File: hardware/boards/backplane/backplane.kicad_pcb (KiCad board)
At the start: 2 copper layers, 47 parts, among them J1 SPARE_I2C, J10 I2C_IN, J11 I2C_OUT, J12 LED_EXT_OUT, J14 DC_IN, J2 SLOT_4, J3 SLOT_1, J4 SLOT_2, J5 SLOT_5, J6 SLOT_6, J7 SLOT_3, J8 LED_EXT_IN, U1 TCA9548APWR, U2 USBLC6-2SC6, U3 USBLC6-2SC6, U4 USBLC6-2SC6, U5 USBLC6-2SC6, U6 USBLC6-2SC6, U7 USBLC6-2SC6

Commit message: Save current PCB layout edits
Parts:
- moved J12 214.8 mm to (196.5, 70.1)
- moved J11 213.7 mm to (196.6, 51.5)
- moved J1 86.8 mm to (54.2, 13.3)
- moved JP3 69.4 mm to (60.3, 32.1), turned to 180 degrees
- moved JP2 67.3 mm to (60.4, 36.2), turned to 180 degrees
- moved JP1 66.9 mm to (60.6, 40.2), turned to 180 degrees
- moved C1 65.8 mm to (57.3, 27.9)
- moved U1 54.3 mm to (52.5, 34.9)
- moved J10 46.0 mm to (19.1, 42.5), turned to 90 degrees
- moved J8 44.3 mm to (20.2, 49.5), turned to 90 degrees
- moved R1 43.2 mm to (45.8, 31.1), turned to -90 degrees

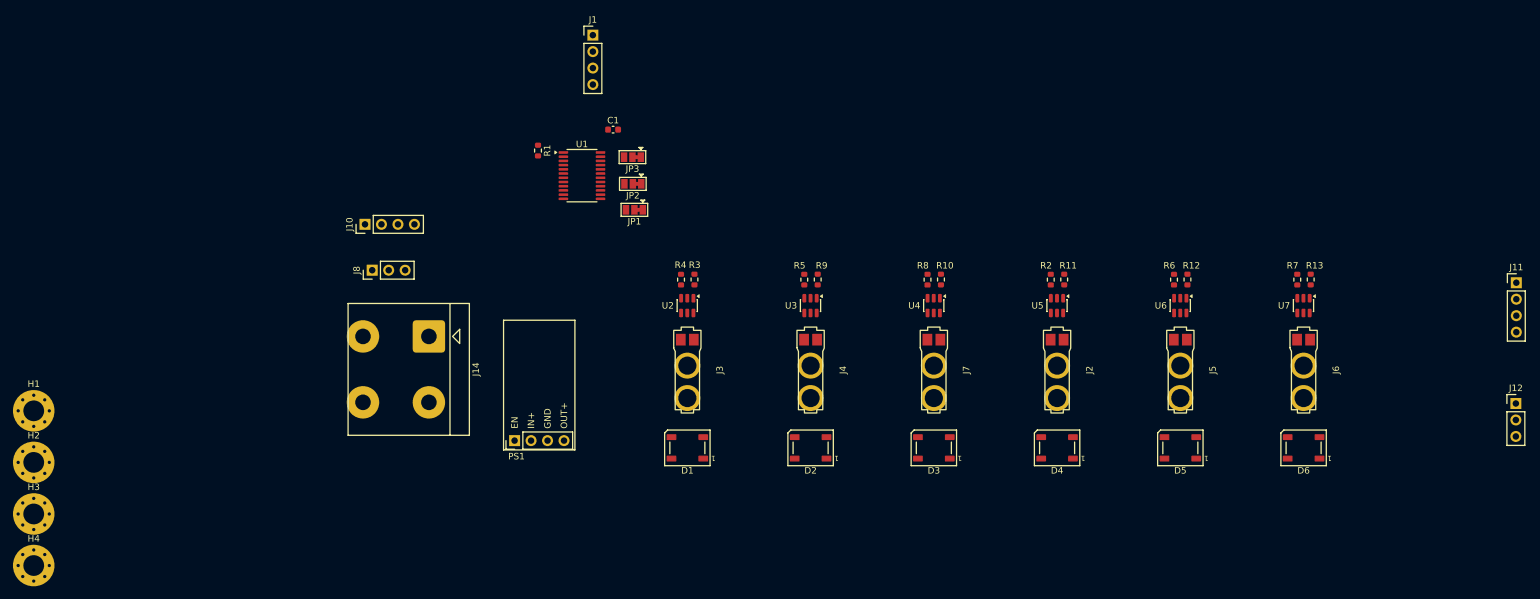
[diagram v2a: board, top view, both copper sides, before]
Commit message: refactor: consolidate active KiCad projects under backplane and carrier
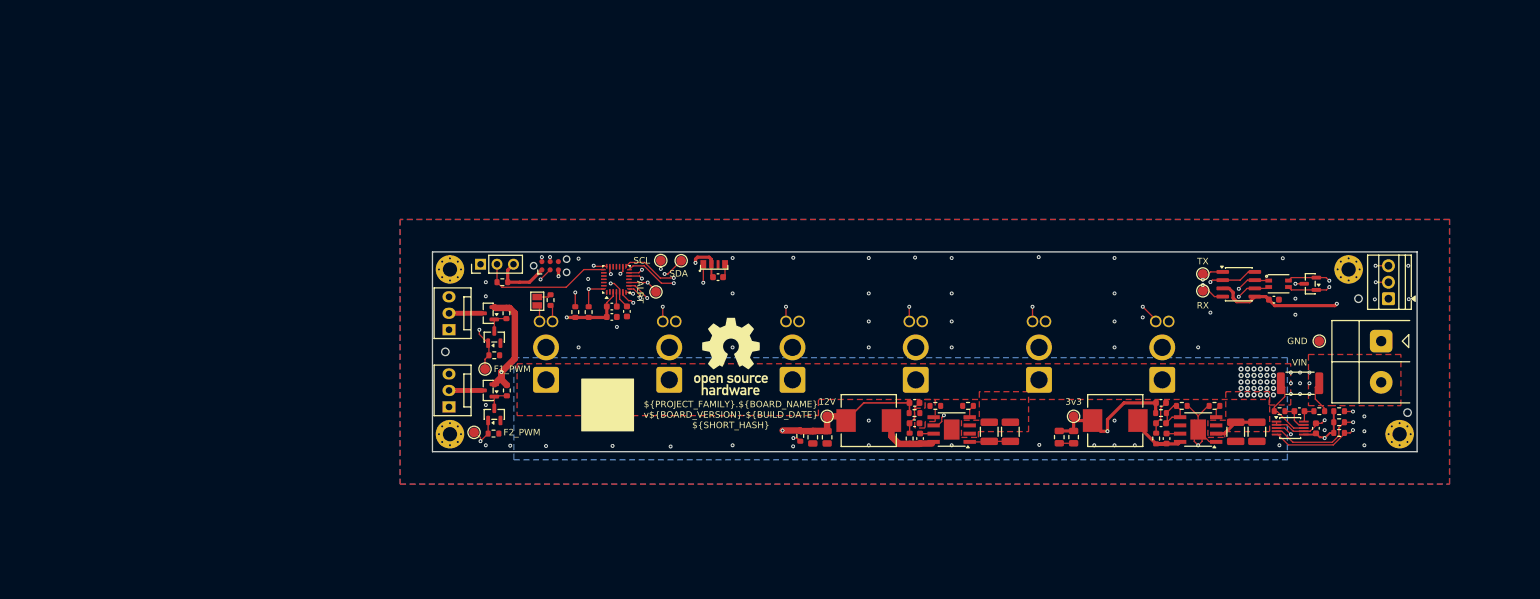
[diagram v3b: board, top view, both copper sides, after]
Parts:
- removed D2: LED_SLOT2, LED_SMD:LED_WS2812B_PLCC4_5.0x5.0mm_P3.2mm
- removed D3: LED_SLOT3, LED_SMD:LED_WS2812B_PLCC4_5.0x5.0mm_P3.2mm
- removed D4: LED_SLOT4, LED_SMD:LED_WS2812B_PLCC4_5.0x5.0mm_P3.2mm
- removed D5: LED_SLOT5, LED_SMD:LED_WS2812B_PLCC4_5.0x5.0mm_P3.2mm
- removed D6: LED_SLOT6, LED_SMD:LED_WS2812B_PLCC4_5.0x5.0mm_P3.2mm
- removed H4: MountingHole_Pad, MountingHole:MountingHole_3.2mm_M3_Pad_Via
- removed J14: DC_IN, mini-rack-power:DEGSON_DG135T-10.16-02P
- removed JP1: A0_ADDR, Jumper:SolderJumper-3_P1.3mm_Bridged12_Pad1.0x1.5mm
- removed JP2: A1_ADDR, Jumper:SolderJumper-3_P1.3mm_Bridged12_Pad1.0x1.5mm
- removed JP3: A2_ADDR, Jumper:SolderJumper-3_P1.3mm_Bridged12_Pad1.0x1.5mm
- removed PS1: Adjustable_DC2DC, mini-rack-power:Adjustable_DC2DC
- removed R5: 47R, Resistor_SMD:R_0603_1608Metric
- removed U6, U7: USBLC6-2SC6, Package_TO_SOT_SMD:SOT-23-6
- added C10: 22uF 25V, Capacitor_SMD:C_0805_2012Metric, F.Cu at (90.3, 75.3)
- added C11: 22uF 25V, Capacitor_SMD:C_0805_2012Metric, F.Cu at (88.1, 75.3)
- added C12: 3.3nF 50V X7R, Capacitor_SMD:C_0603_1608Metric, F.Cu at (103.8, 70.0)
- added C13: 56pF 50V C0G, Capacitor_SMD:C_0603_1608Metric, F.Cu at (103.8, 73.1)
- added C14: 22uF 25V, Capacitor_SMD:C_0805_2012Metric, F.Cu at (126.1, 75.2)
- added C15: 100nF, Capacitor_SMD:C_0603_1608Metric, F.Cu at (163.2, 71.3)
- added C16: 100nF, Capacitor_SMD:C_0603_1608Metric, F.Cu at (165.7, 73.9)
- added C17: 100nF, Capacitor_SMD:C_0603_1608Metric, F.Cu at (57.2, 56.7)
- added C18: 4.7uF, Capacitor_SMD:C_0603_1608Metric, F.Cu at (57.2, 55.1)
- added C19: 100nF, Capacitor_SMD:C_0603_1608Metric, F.Cu at (59.5, 55.9)
- added C2: 2.2uF 100V, Capacitor_SMD:C_1210_3225Metric, F.Cu at (153.3, 74.4)
- added C20: 100nF, Capacitor_SMD:C_0603_1608Metric, F.Cu at (159.2, 54.1)
- added C21: 100nF, Capacitor_SMD:C_0603_1608Metric, F.Cu at (73.5, 50.6)
- added C3: 2.2nF 50V, Capacitor_SMD:C_0603_1608Metric, F.Cu at (142.7, 75.5)
- added C4: 22uF 25V, Capacitor_SMD:C_0805_2012Metric, F.Cu at (128.3, 75.2)
- added C5: 2.2nF 50V, Capacitor_SMD:C_0603_1608Metric, F.Cu at (141.8, 70.0)
- added C6: 220pF C0G, Capacitor_SMD:C_0603_1608Metric, F.Cu at (141.8, 73.1)
- added C7: 2.2uF 100V, Capacitor_SMD:C_1210_3225Metric, F.Cu at (118.6, 74.4)
- added C8: 2.2uF 100V, Capacitor_SMD:C_1210_3225Metric, F.Cu at (115.3, 74.4)
- added C9: 2.2nF 50V, Capacitor_SMD:C_0603_1608Metric, F.Cu at (104.7, 75.5)
- added H5: M2 CHASSIS, mini-rack-power:MountingHole_2.2mm_M2_Pad_Via_JLC, B.Cu at (32.2, 74.8)
- added H7: ToolingHole_1.152mm, mini-rack-power:MountingHole_JLCPCB_Tooling_1.152mm, F.Cu at (31.5, 62.1)
- added H8: ToolingHole_1.152mm, mini-rack-power:MountingHole_JLCPCB_Tooling_1.152mm, F.Cu at (179.8, 71.5)
- added H9: ToolingHole_1.152mm, mini-rack-power:MountingHole_JLCPCB_Tooling_1.152mm, F.Cu at (172.3, 53.9)
- added J9: 12V 3-WIRE FAN, Connector_MiniRackPower:FanPinHeader_1x03_P2.54mm_Vertical_JLC_Edge, F.Cu at (32.0, 58.7)
- added L1: 100uH, mini-rack-power:L_PRODTech_PSPMAA0805, F.Cu at (134.8, 72.7)
- added L2: 100uH, mini-rack-power:L_PRODTech_PSPMAA0805, F.Cu at (96.8, 72.7)
- added L3: ACT1210D-101-2P-TL00, mini-rack-power:L_CommonModeChoke_TDK_ACT1210D, F.Cu at (159.9, 51.6)
- added LED1: WS2812B-4020-V6, mini-rack-power:LED_Worldsemi_WS2812B-4020-V6_SideView, F.Cu at (72.9, 48.0)
- added Q1: AO3407A, Package_TO_SOT_SMD:SOT-23, F.Cu at (38.1, 56.2)
- added Q2: 2N7002, Package_TO_SOT_SMD:SOT-23, F.Cu at (39.0, 59.8)
- added Q3: AO3407A, Package_TO_SOT_SMD:SOT-23, F.Cu at (38.1, 68.1)
- added Q4: 2N7002, Package_TO_SOT_SMD:SOT-23, F.Cu at (39.0, 71.8)
- added R14: 2.2k, Resistor_SMD:R_0603_1608Metric, F.Cu at (169.3, 74.6)
- added R15: 10k, Resistor_SMD:R_0603_1608Metric, F.Cu at (169.3, 71.3)
- added R17: 120R 1%, Resistor_SMD:R_0603_1608Metric, F.Cu at (47.7, 54.1)
- added R18: 100k 1%, Resistor_SMD:R_0603_1608Metric, F.Cu at (40.9, 56.2)
- added R19: 100k 1%, Resistor_SMD:R_0603_1608Metric, F.Cu at (39.0, 62.6)
- added R20: 10k, Resistor_SMD:R_0603_1608Metric, F.Cu at (53.6, 56.0)
- added R21: 100k 1%, Resistor_SMD:R_0603_1608Metric, F.Cu at (41.0, 68.1)
- added R22: 100k 1%, Resistor_SMD:R_0603_1608Metric, F.Cu at (38.9, 74.7)
- added R23: 10k, Resistor_SMD:R_0603_1608Metric, F.Cu at (51.5, 56.0)
- added R24: 4.7k 1%, Resistor_SMD:R_0603_1608Metric, F.Cu at (40.3, 51.4)
- added REF**: OSHW-Logo_11.4x12mm_SilkScreen, Symbol:OSHW-Logo_11.4x12mm_SilkScreen, F.Cu at (75.5, 62.8)
- added RSH1: 1mR 1% 6W, Resistor_SMD:R_2512_6332Metric, F.Cu at (163.2, 67.0)
- added SJ1: TERMINATION, Jumper:SolderJumper-2_P1.3mm_Open_Pad1.0x1.5mm, F.Cu at (45.7, 54.3)
- added TP10: INA_ALERT, TestPoint:TestPoint_Pad_D1.5mm, F.Cu at (64.0, 52.9)
- added TP12: FAN_PWM, TestPoint:TestPoint_Pad_D1.5mm, F.Cu at (35.9, 74.5)
- added TP13: FAN_PWM, TestPoint:TestPoint_Pad_D1.5mm, F.Cu at (37.6, 64.8)
- added TP3: +3V3, TestPoint:TestPoint_Pad_D1.5mm, F.Cu at (128.3, 72.0)
- added TP4: +12V, TestPoint:TestPoint_Pad_D1.5mm, F.Cu at (90.3, 72.0)
- added TP5: GND, TestPoint:TestPoint_Pad_D1.5mm, F.Cu at (166.2, 60.5)
- added TP6: CAN_TX, TestPoint:TestPoint_Pad_D1.5mm, F.Cu at (148.3, 50.1)
- added TP7: CAN_RX, TestPoint:TestPoint_Pad_D1.5mm, F.Cu at (148.3, 52.7)
- added TP8: I2C_SDA, TestPoint:TestPoint_Pad_D1.5mm, F.Cu at (67.8, 48.1)
- added TP9: I2C_SCL, TestPoint:TestPoint_Pad_D1.5mm, F.Cu at (64.7, 48.0)
- C1: value 100nF -> 2.2uF 100V; footprint Capacitor_SMD:C_0603_1608Metric -> Capacitor_SMD:C_1210_3225Metric
- D1: value LED_SLOT1 -> PESD2CANFD27V-TR; footprint LED_SMD:LED_WS2812B_PLCC4_5.0x5.0mm_P3.2mm -> Package_TO_SOT_SMD:SOT-23
- H1, H2, H3: value MountingHole_Pad -> M2 CHASSIS; footprint MountingHole:MountingHole_3.2mm_M3_Pad_Via -> mini-rack-power:MountingHole_2.2mm_M2_Pad_Via_JLC; moved to B.Cu
- J1: value SPARE_I2C -> XT30U_2+2; footprint Connector_PinHeader_2.54mm:PinHeader_1x04_P2.54mm_Vertical -> mini-rack-power:Amass_XT30U_2plus2_F; moved to B.Cu
- J10: value I2C_IN -> SWD; footprint Connector_PinHeader_2.54mm:PinHeader_1x04_P2.54mm_Vertical -> Connector:Tag-Connect_TC2030-IDC-NL_2x03_P1.27mm_Vertical
- J11: value I2C_OUT -> 12V 3-WIRE FAN; footprint Connector_PinHeader_2.54mm:PinHeader_1x04_P2.54mm_Vertical -> Connector_MiniRackPower:FanPinHeader_1x03_P2.54mm_Vertical_JLC_Edge
- J12: value LED_EXT_OUT -> DS18B20 EXT SUPPLY
- J2: value SLOT_4 -> XT30U_2+2; moved to B.Cu
- J3: value SLOT_1 -> XT30U_2+2; moved to B.Cu
- J4: value SLOT_2 -> XT30U_2+2; moved to B.Cu
- J5: value SLOT_5 -> XT30U_2+2; moved to B.Cu
- J6: value SLOT_6 -> XT30U_2+2; moved to B.Cu
- J7: value SLOT_3 -> XY308-2.54-3P / EXTERNAL CAN; footprint mini-rack-power:Amass_XT30U_2plus2_F -> mini-rack-power:TerminalBlock_Xinya_XY308-2.54-3P_1x03_P2.54mm_Horizontal
- J8: value LED_EXT_IN -> DC IN; footprint Connector_PinHeader_2.54mm:PinHeader_1x03_P2.54mm_Vertical -> mini-rack-power:DORABO_DB910-6.35-2P-GN-S
- R1: value 10k -> 27k 1%
- R10: value 47R -> 10k
- R11, R12: value 47R -> 10R
- R13: value 47R -> 2.2k
- R2, R4: value 47R -> 110k 1%
- R3: value 47R -> 62k 1%
- R6: value 47R -> 100k 1%
- R7, R9: value 47R -> 453k 1%
- R8: value 47R -> 49.9k 1%
- U1: value TCA9548APWR -> STM32C092GCU6; footprint Package_SO:TSSOP-24_4.4x7.8mm_P0.65mm -> Package_DFN_QFN:QFN-28_4x4mm_P0.5mm
- U2, U3: value USBLC6-2SC6 -> LM5164DDAR; footprint Package_TO_SOT_SMD:SOT-23-6 -> Package_SO:TI_SO-PowerPAD-8
- U4: value USBLC6-2SC6 -> INA237AIDGSR; footprint Package_TO_SOT_SMD:SOT-23-6 -> mini-rack-power:MSOP-10_3x3mm_P0.5mm_0.20mm_Clearance
- U5: value USBLC6-2SC6 -> TCAN3413DR; footprint Package_TO_SOT_SMD:SOT-23-6 -> Package_SO:SOIC-8_3.9x4.9mm_P1.27mm
- moved H2 210.6 mm to (178.6, 74.8), turned to 180 degrees
- moved H1 203.9 mm to (170.7, 49.4), turned to 180 degrees
- moved J11 165.7 mm to (32.0, 70.6), turned to 90 degrees
- moved J12 161.0 mm to (36.9, 48.6), turned to 90 degrees
- moved J8 156.2 mm to (175.8, 63.6), turned to -90 degrees
- moved J6 116.8 mm to (47.0, 62.1)
- moved R1 111.5 mm to (150.1, 70.4), turned to 180 degrees
- moved C1 109.6 mm to (156.6, 74.4), turned to -90 degrees
- moved J1 100.4 mm to (142.0, 62.1), turned to -90 degrees
- moved D1 99.3 mm to (164.8, 51.6)
- moved U2 81.0 mm to (147.5, 74.1), turned to 180 degrees
- moved J5 78.8 mm to (66.0, 62.1)
- moved R3 77.6 mm to (145.0, 70.4), turned to 0 degrees
- moved R4 77.2 mm to (141.1, 75.5), turned to 90 degrees
- moved H3 74.4 mm to (32.2, 49.4), turned to 180 degrees
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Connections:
- C1 pad 1: +3V3 -> VCC
- D1 pad 1: +5V -> /CAN-FD and Six Slots/CAN_EXT_N
- D1 pad 2: Net-(D1-DOUT) -> /CAN-FD and Six Slots/CAN_EXT_P
- J1 pad 1: Net-(J1-Pin_1) -> VCC
- J1 pad 2: Net-(J1-Pin_2) -> GND
- J1 pad 3: Net-(J1-Pin_3) -> /CAN-FD and Six Slots/CAN_BUS_P
- J1 pad 4: Net-(J1-Pin_4) -> /CAN-FD and Six Slots/CAN_BUS_N
- J10 pad 1: GND -> +3V3
- J10 pad 2: I2C_UP_SCL -> /MCU and Local Control/SWDIO
- J10 pad 3: I2C_UP_SDA -> /MCU and Local Control/NRST
- J10 pad 4: +3V3 -> /MCU and Local Control/SWCLK
- J11 pad 2: I2C_UP_SCL -> /Fan Control and Status/FAN2_12V_SW
- J11 pad 3: I2C_UP_SDA -> FAN2_TACH
- J12 pad 2: /Slots and LEDs/LED_DOUT -> DS18B20_DATA
- J12 pad 3: +5V -> +3V3
- J2 pad 1: +24V -> VCC
- J2 pad 3: Net-(J2-Pin_3) -> /CAN-FD and Six Slots/CAN_BUS_P
- J2 pad 4: Net-(J2-Pin_4) -> /CAN-FD and Six Slots/CAN_BUS_N
- J3 pad 1: +24V -> VCC
- J3 pad 3: Net-(J3-Pin_3) -> /CAN-FD and Six Slots/CAN_BUS_P
- J3 pad 4: Net-(J3-Pin_4) -> /CAN-FD and Six Slots/CAN_BUS_N
- J4 pad 1: +24V -> VCC
- J4 pad 3: Net-(J4-Pin_3) -> /CAN-FD and Six Slots/CAN_BUS_P
- J4 pad 4: Net-(J4-Pin_4) -> /CAN-FD and Six Slots/CAN_BUS_N
- J5 pad 1: +24V -> VCC
- J5 pad 3: Net-(J5-Pin_3) -> /CAN-FD and Six Slots/CAN_BUS_P
- J5 pad 4: Net-(J5-Pin_4) -> /CAN-FD and Six Slots/CAN_BUS_N
- J6 pad 1: +24V -> VCC
- J6 pad 3: Net-(J6-Pin_3) -> /CAN-FD and Six Slots/CAN_BUS_P
- J6 pad 4: Net-(J6-Pin_4) -> /CAN-FD and Six Slots/CAN_BUS_N
- J7 pad 1: +24V -> GND
- J7 pad 2: GND -> /CAN-FD and Six Slots/CAN_EXT_N
- J7 pad 3: Net-(J7-Pin_3) -> /CAN-FD and Six Slots/CAN_EXT_P
- J8 pad 2: /Slots and LEDs/LED_DATA_IN -> VIN_RAW
- R1 pad 1: +3V3 -> Net-(U2-RON)
- R1 pad 2: Net-(U1-~{RESET}) -> GND
- R10 pad 1: SCL_SLOT_3 -> +12V
- R10 pad 2: Net-(R10-Pad2) -> PGOOD_12V
- R11 pad 1: SCL_SLOT_4 -> VIN_RAW
- R11 pad 2: Net-(R11-Pad2) -> /Power Input and Monitor/INA_IN_P
- R12 pad 1: SCL_SLOT_5 -> VCC
- R12 pad 2: Net-(R12-Pad2) -> /Power Input and Monitor/INA_IN_N
- R13 pad 1: SCL_SLOT_6 -> +3V3
- R13 pad 2: Net-(R13-Pad2) -> I2C_SDA
- R2 pad 1: SDA_SLOT_4 -> +3V3
- R2 pad 2: Net-(R2-Pad2) -> /Buck Converters/FB_3V3
- R3 pad 1: SCL_SLOT_1 -> /Buck Converters/FB_3V3
- R3 pad 2: Net-(R3-Pad2) -> GND
- R4 pad 1: SDA_SLOT_1 -> /Buck Converters/SW_3V3
- R4 pad 2: Net-(R4-Pad2) -> /Buck Converters/RIPPLE_3V3
- R6 pad 1: SDA_SLOT_5 -> Net-(U3-RON)
- R6 pad 2: Net-(R6-Pad2) -> GND
- R7 pad 1: SDA_SLOT_6 -> +12V
- R7 pad 2: Net-(R7-Pad2) -> /Buck Converters/FB_12V
- R8 pad 1: SDA_SLOT_3 -> /Buck Converters/FB_12V
- R8 pad 2: Net-(R8-Pad2) -> GND
- R9 pad 1: SCL_SLOT_2 -> /Buck Converters/SW_12V
- R9 pad 2: Net-(R9-Pad2) -> /Buck Converters/RIPPLE_12V
- U1 pad 1: /I2C Mux/TCA9548A_A0 -> unconnected-(U1-PC14-Pad1)
- U1 pad 10: SDA_SLOT_4 -> INA_ALERT
- U1 pad 11: SCL_SLOT_4 -> unconnected-(U1-PA5-Pad11)
- U1 pad 12: GND -> I2C_SDA
- U1 pad 13: SDA_SLOT_5 -> I2C_SCL
- U1 pad 14: SCL_SLOT_5 -> CAN_RX
- U1 pad 15: SDA_SLOT_6 -> CAN_TX
- U1 pad 16: SCL_SLOT_6 -> FAN2_TACH
- U1 pad 17: Net-(J1-Pin_2) -> unconnected-(U1-PC6-Pad17)
- U1 pad 18: Net-(J1-Pin_1) -> unconnected-(U1-PA9/PA11-Pad18)
- U1 pad 19: Net-(J1-Pin_4) -> unconnected-(U1-PA10/PA12-Pad19)
- U1 pad 2: /I2C Mux/TCA9548A_A1 -> unconnected-(U1-PC15-Pad2)
- U1 pad 20: Net-(J1-Pin_3) -> /MCU and Local Control/SWDIO
- U1 pad 21: /I2C Mux/TCA9548A_A2 -> /MCU and Local Control/SWCLK
- U1 pad 22: I2C_UP_SCL -> DS18B20_DATA
- U1 pad 23: I2C_UP_SDA -> unconnected-(U1-PB3-Pad23)
- U1 pad 24: +3V3 -> unconnected-(U1-PB4-Pad24)
- U1 pad 3: Net-(U1-~{RESET}) -> +3V3
- U1 pad 4: SDA_SLOT_1 -> GND
- U1 pad 5: SCL_SLOT_1 -> /MCU and Local Control/NRST
- U1 pad 6: SDA_SLOT_2 -> FAN2_PWM
- U1 pad 7: SCL_SLOT_2 -> /MCU and Local Control/LED_DATA_RAW
- U1 pad 8: SDA_SLOT_3 -> FAN_PWM
- U1 pad 9: SCL_SLOT_3 -> PGOOD_12V
- U2 pad 1: Net-(R3-Pad2) -> GND
- U2 pad 2: GND -> VCC
- U2 pad 3: Net-(R4-Pad2) -> VCC
- U2 pad 4: Net-(J3-Pin_4) -> Net-(U2-RON)
- U2 pad 5: +3V3 -> /Buck Converters/FB_3V3
- U2 pad 6: Net-(J3-Pin_3) -> unconnected-(U2-PGOOD-Pad6)
- U3 pad 1: Net-(R9-Pad2) -> GND
- U3 pad 2: GND -> VCC
- U3 pad 3: Net-(R5-Pad2) -> VCC
- U3 pad 4: Net-(J4-Pin_4) -> Net-(U3-RON)
- U3 pad 5: +3V3 -> /Buck Converters/FB_12V
- U3 pad 6: Net-(J4-Pin_3) -> PGOOD_12V
- U4 pad 1: Net-(R10-Pad2) -> GND
- U4 pad 3: Net-(R8-Pad2) -> INA_ALERT
- U4 pad 4: Net-(J7-Pin_4) -> I2C_SDA
- U4 pad 5: +3V3 -> I2C_SCL
- U4 pad 6: Net-(J7-Pin_3) -> +3V3
- U5 pad 1: Net-(R11-Pad2) -> CAN_TX
- U5 pad 3: Net-(R2-Pad2) -> +3V3
- U5 pad 4: Net-(J2-Pin_4) -> CAN_RX
- U5 pad 6: Net-(J2-Pin_3) -> /CAN-FD and Six Slots/CAN_BUS_N
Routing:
- net +3V3: track 0.00 -> 290.0 mm, vias 0 -> 5
- net I2C_SDA: track 0.00 -> 160.9 mm, vias 0 -> 3
- net I2C_SCL: track 0.00 -> 159.2 mm, vias 0 -> 3
- net INA_ALERT: track 0.00 -> 158.0 mm, vias 0 -> 3
- net /CAN-FD and Six Slots/CAN_BUS_P: track 0.00 -> 132.4 mm, vias 0 -> 6
- net /CAN-FD and Six Slots/CAN_BUS_N: track 0.00 -> 125.7 mm, vias 0 -> 2
- net PGOOD_12V: track 0.00 -> 117.1 mm, vias 0 -> 3
- net CAN_RX: track 0.00 -> 94.3 mm, vias 0 -> 2
- net CAN_TX: track 0.00 -> 94.0 mm, vias 0 -> 2
- net +12V: track 0.00 -> 93.7 mm, vias 0 -> 2
- net FAN2_PWM: track 0.00 -> 48.6 mm, vias 0 -> 2
- net GND: track 0.00 -> 48.4 mm, vias 0 -> 68
- net FAN2_TACH: track 0.00 -> 41.8 mm, vias 0 -> 2
- net FAN_PWM: track 0.00 -> 36.5 mm, vias 0 -> 2
- net FAN_TACH: track 0.00 -> 27.0 mm, vias 0 -> 1
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- added copper zone on F.Cu, net /Buck Converters/FB_12V
- added copper zone on B.Cu, net GND
- added copper zone on F.Cu, net GND
- added copper zone on In1.Cu, net GND
- added copper zone on In2.Cu, net GND
- added copper zone on B.Cu, net VCC
- added copper zone on F.Cu, net VCC
- added copper zone on In1.Cu, net VCC
- added copper zone on In2.Cu, net VCC
- added copper zone on F.Cu, net VIN_RAW
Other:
- board outline added: 151.8 x 30.8 mm
- copper layers 2 -> 4
- board text added: "${PROJECT_FAMILY}.${BOARD_NAME} v${BOARD_VERSION}-${BUILD_DATE} ${SHORT_HASH}"
- board text added: "+"
- board text added: "-"
- board text added: "12V"
- board text added: "3v3"
- board text added: "ALRT"
- board text added: "F1_PWM"
- board text added: "F2_PWM"
- board text added: "G"
- board text added: "GND"
- board text added: "RX"
- board text added: "S01"
- board text added: "S02"
- board text added: "S03"
- board text added: "S04"
- board text added: "S05"
- board text added: "S06"
- board text added: "SCL"
- board text added: "SDA"
- board text added: "TX"
- board text added: "VIN"

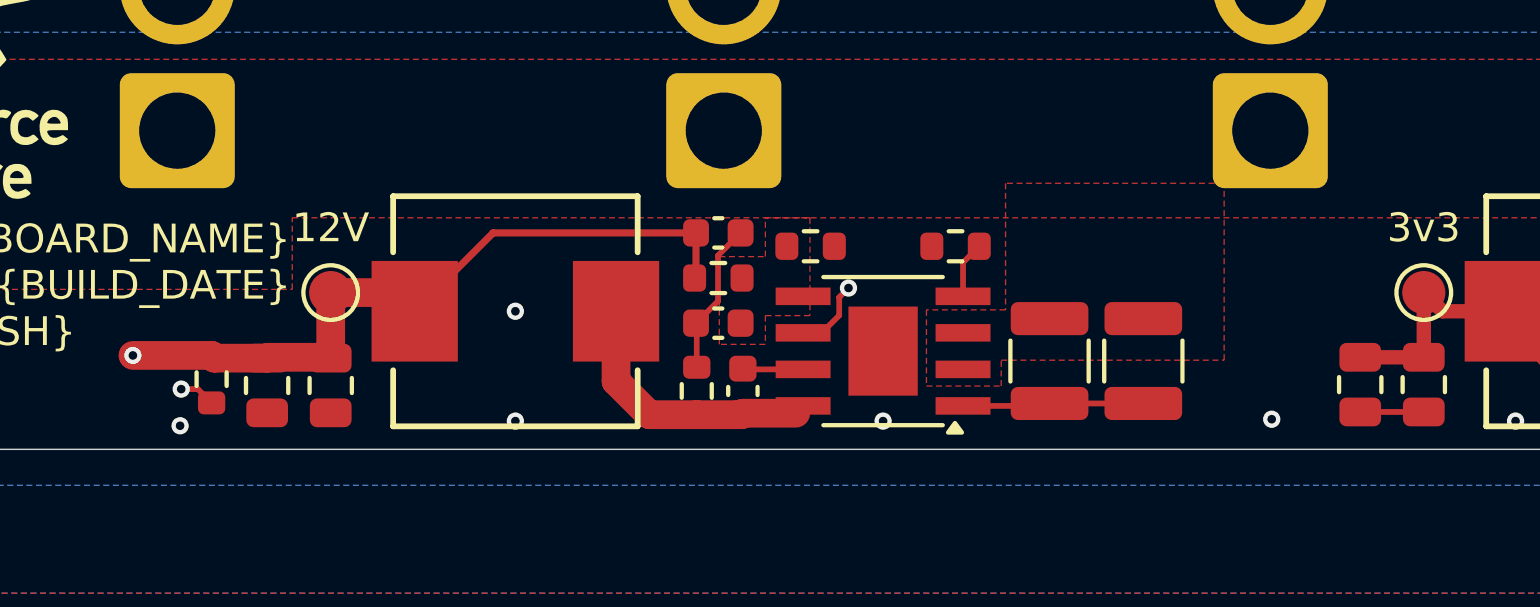
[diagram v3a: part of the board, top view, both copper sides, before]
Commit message: Checkpoint current board layouts before 12V buck review
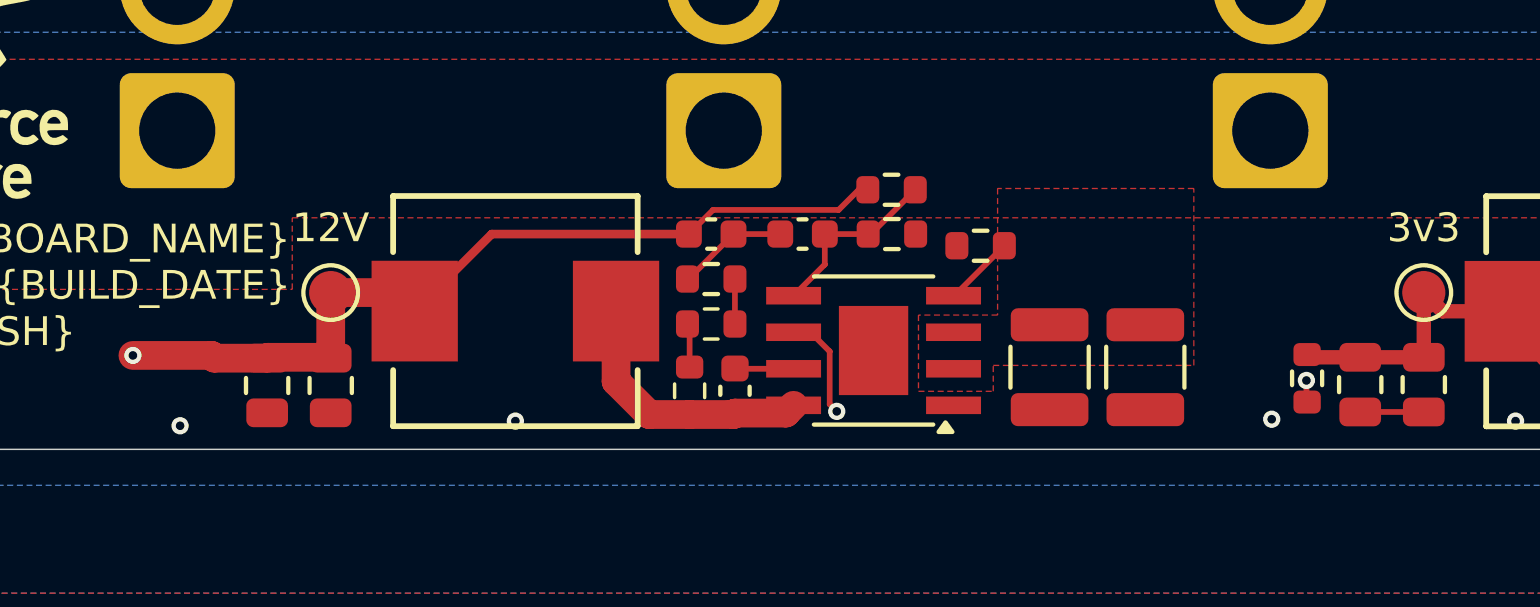
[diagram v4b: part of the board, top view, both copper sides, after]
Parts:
- added R25: 110k 1%, Resistor_SMD:R_0603_1608Metric, F.Cu at (103.6, 73.1)
- added R26: 110k 1%, Resistor_SMD:R_0603_1608Metric, F.Cu at (102.8, 75.5)
- C12: value 3.3nF 50V X7R -> 2.2nF 50V
- R9: value 453k 1% -> 110k 1%
- moved R10 38.1 mm to (124.3, 75.0)
- moved R7 6.76 mm to (109.8, 68.5)
- moved C13 4.26 mm to (106.7, 70.0)
- moved R9 3.92 mm to (103.6, 71.6), turned to 180 degrees
- moved R8 2.86 mm to (109.8, 70.0)
- moved R6 0.87 mm to (112.9, 70.4)
- moved U3 0.33 mm to (109.2, 74.1)
- moved C9 0.27 mm to (104.4, 75.5)
- moved C12 0.25 mm to (103.6, 70.0)
- moved C7 0.22 mm to (118.7, 74.6)
- moved C8 0.21 mm to (115.3, 74.6)
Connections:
- R10 pad 1: +12V -> +3V3
- R9 pad 1: /Buck Converters/SW_12V -> Net-(R25-Pad2)
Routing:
- net PGOOD_12V: track 117.1 -> 132.9 mm
- net GND: track 48.4 -> 39.9 mm, vias 68 -> 66
- net /Buck Converters/FB_12V: track 0.07 -> 6.61 mm
- net +12V: track 93.7 -> 97.8 mm
- net +3V3: track 290.0 -> 291.9 mm
- net Net-(R25-Pad2): track 0.00 -> 1.56 mm
- net Net-(R25-Pad1): track 0.00 -> 1.50 mm
- net /Buck Converters/RIPPLE_12V: track 5.32 -> 3.87 mm
- net Net-(U3-RON): track 1.97 -> 2.49 mm
- removed copper zone on F.Cu, net /Buck Converters/FB_12V

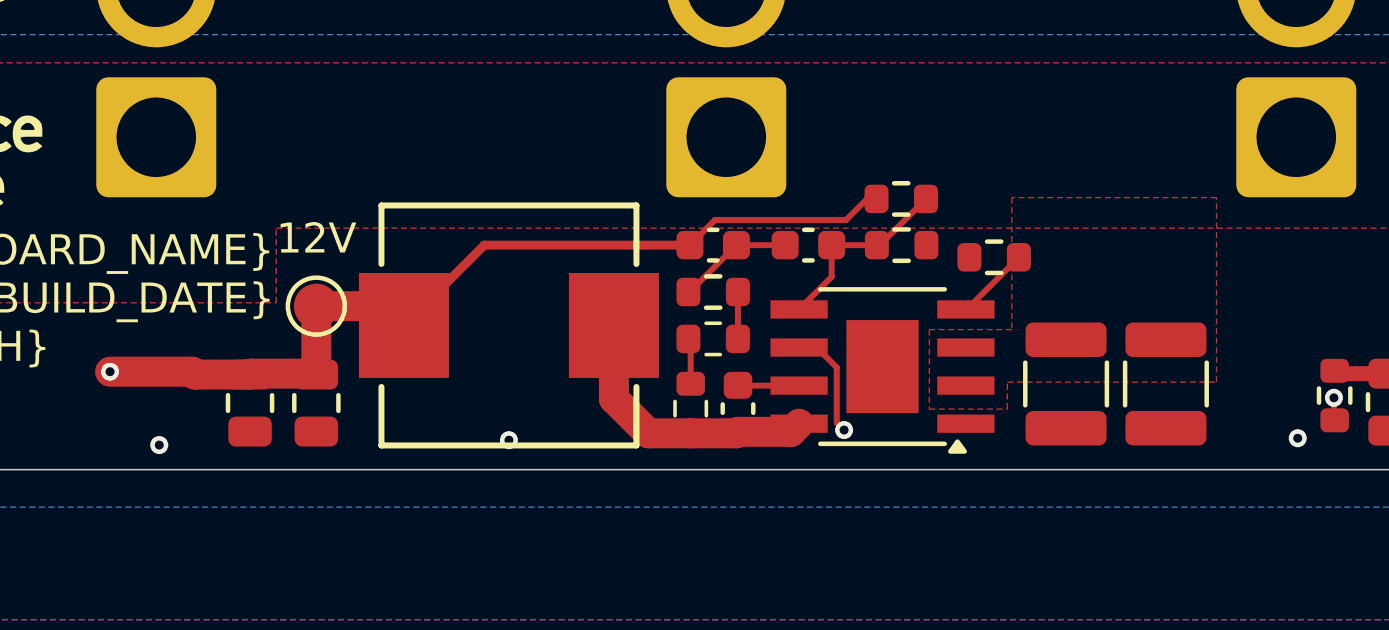
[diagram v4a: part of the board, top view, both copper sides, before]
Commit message: Match 12V buck placement and local routing to 3V3 buck
Preserve 12V component values and reconnect PGOOD and output distribution. Translate the template left to clear the existing PGOOD via and J3. Remove obsolete R25/R26 footprints.

Validation: 14 corresponding placements and 55 local traces match the source template; DRC has zero errors and zero unrouted connections. Footprint library mismatch warnings remain for U3 and TP4.
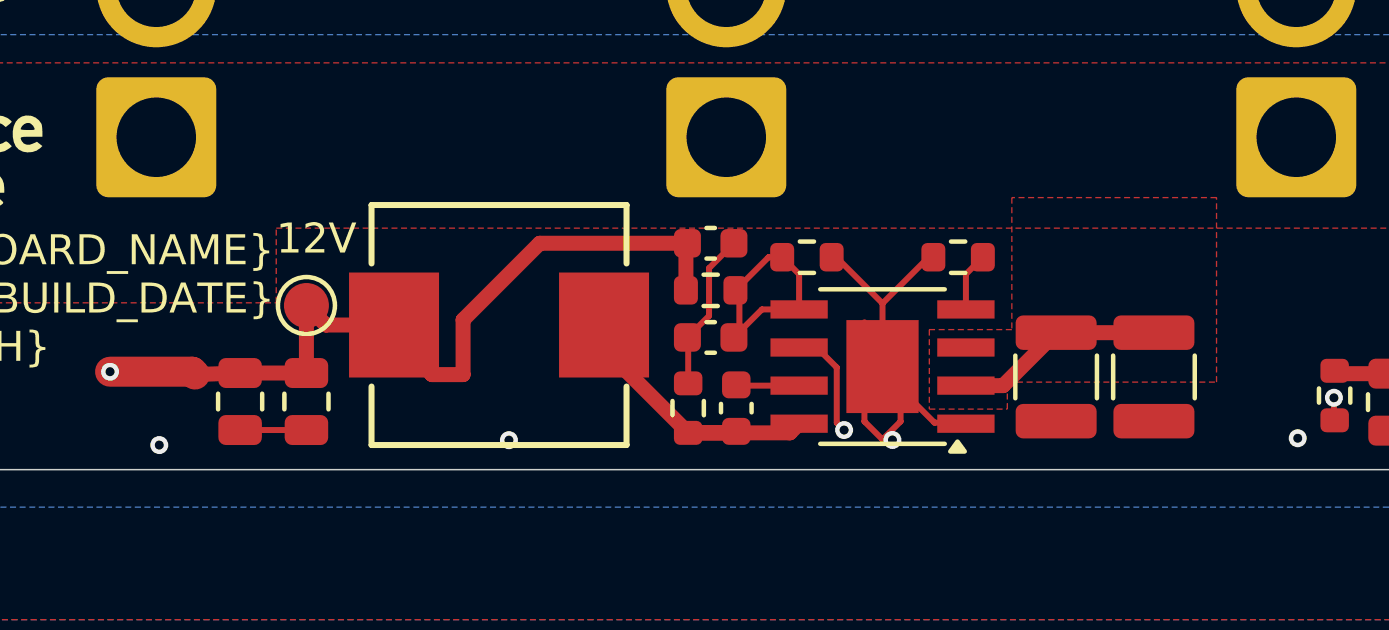
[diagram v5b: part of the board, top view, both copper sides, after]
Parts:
- removed R25, R26: 110k 1%, Resistor_SMD:R_0603_1608Metric
- R9: value 110k 1% -> 330k 1%
- moved R7 7.05 mm to (103.5, 71.5)
- moved C13 4.48 mm to (103.5, 73.1)
- moved R9 3.96 mm to (102.7, 75.4), turned to 90 degrees
- moved R8 3.18 mm to (106.7, 70.4)
- moved R6 1.20 mm to (111.7, 70.4)
- moved C7 0.46 mm to (118.3, 74.4)
- moved C8 0.41 mm to (115.0, 74.4)
- moved C10 0.33 mm to (90.0, 75.2)
- moved C11 0.33 mm to (87.8, 75.2)
- moved TP4 0.33 mm to (90.0, 72.0)
- moved L2 0.33 mm to (96.4, 72.7)
- moved C12 0.10 mm to (103.5, 70.0)
- moved C9 0.06 mm to (104.3, 75.4)
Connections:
- R9 pad 1: Net-(R25-Pad2) -> /Buck Converters/SW_12V
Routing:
- net GND: track 39.9 -> 56.7 mm, vias 66 -> 67
- net VCC: track 17.9 -> 24.9 mm
- net +12V: track 97.8 -> 96.0 mm
- net /Buck Converters/FB_12V: track 6.61 -> 8.25 mm
- net Net-(R25-Pad2): track 1.56 -> 0.00 mm
- net Net-(R25-Pad1): track 1.50 -> 0.00 mm
- net /Buck Converters/RIPPLE_12V: track 3.87 -> 5.32 mm
- net /Buck Converters/SW_12V: track 9.22 -> 10.4 mm
- net Net-(U3-RON): track 2.49 -> 1.94 mm
